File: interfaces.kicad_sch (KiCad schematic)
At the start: 120 parts, among them J6001 HDMI-A_WE_685119134923, J6002 USB-C_USB4105-GF-A, J6003 MicroSD_693071020811, Q6001 BSS138PW, Q6002 BSS138PW, Q6003 BSS138PW, Q6004 BSS138PW, Q6005 BSS138PW, Q6006 BSS138PW, Q6007 BSS138PW, Q6008 BSS138PW, SW6001 SW_KMR211NGLFS_SMD, U6001 FT4232H_VQFN, Y6001 Oscillator_SMD_12MHz_KX-7

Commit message: Sync new components with PCB
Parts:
- removed C? (x2): C_100n_0402_EIA, K410T-devboard-footprints:C_0402_1005Metric_EIA, symbol K410T-devboard:C_100n_0402_EIA
- removed FB?: FB_120Z_2A_0603, K410T-devboard-footprints:FB_0603_1608Metric, symbol K410T-devboard:FB_120Z_2A_0603
- added C6020, C6021: C_100n_0402, antmicro-footprints:C_0402_1005Metric, symbol antmicroCapacitors0402:C_100n_0402
- added FB6003: FB_120Z_2A_Murata-BLM18PG_0603, antmicro-footprints:FB_0603_1608Metric, symbol antmicroFerriteBeadsandChips:FB_120Z_2A_Murata-BLM18PG_0603
- gave numbers to parts that had none: 27
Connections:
- net +5V: now also FB6003.1
- net FTDI_3V3: now also C6021.2
- net GND: now also C6020.1, C6021.1
- net HDMI_5V: now also C6020.2, FB6003.2

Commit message: Continue optimizing placement and layout of misc. circuitry
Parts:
- added C6022, C6023, C6024, C6025: C_100n_0402, antmicro-footprints:C_0402_1005Metric, symbol antmicroCapacitors0402:C_100n_0402
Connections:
- net +3V3: now also C6024.2, C6025.2; no longer C6005.1, C6008.1, C6009.1, C6010.1
- net DBG_USB_N: now also U6004.4, U6004.7; no longer U6004.2, U6004.9
- net DBG_USB_P: now also U6004.2, U6004.9; no longer U6004.1, U6004.10
- net FTDI_3V3: now also C6005.1, C6008.1, C6009.1, C6010.1, C6022.2, C6023.2
- net FTDI_JTAG_TCK: now also U6003.3 (A2); no longer U6003.2 (A1)
- net FTDI_JTAG_TMS: now also U6003.2 (A1); no longer U6003.3 (A2)
- net GND: now also C6022.1, C6023.1, C6024.1, C6025.1
- net TCK_JTAG: now also R6011.2; no longer R6008.2
- net TMS_JTAG: now also R6008.2; no longer R6011.2
- new net: U6004.1, U6004.10

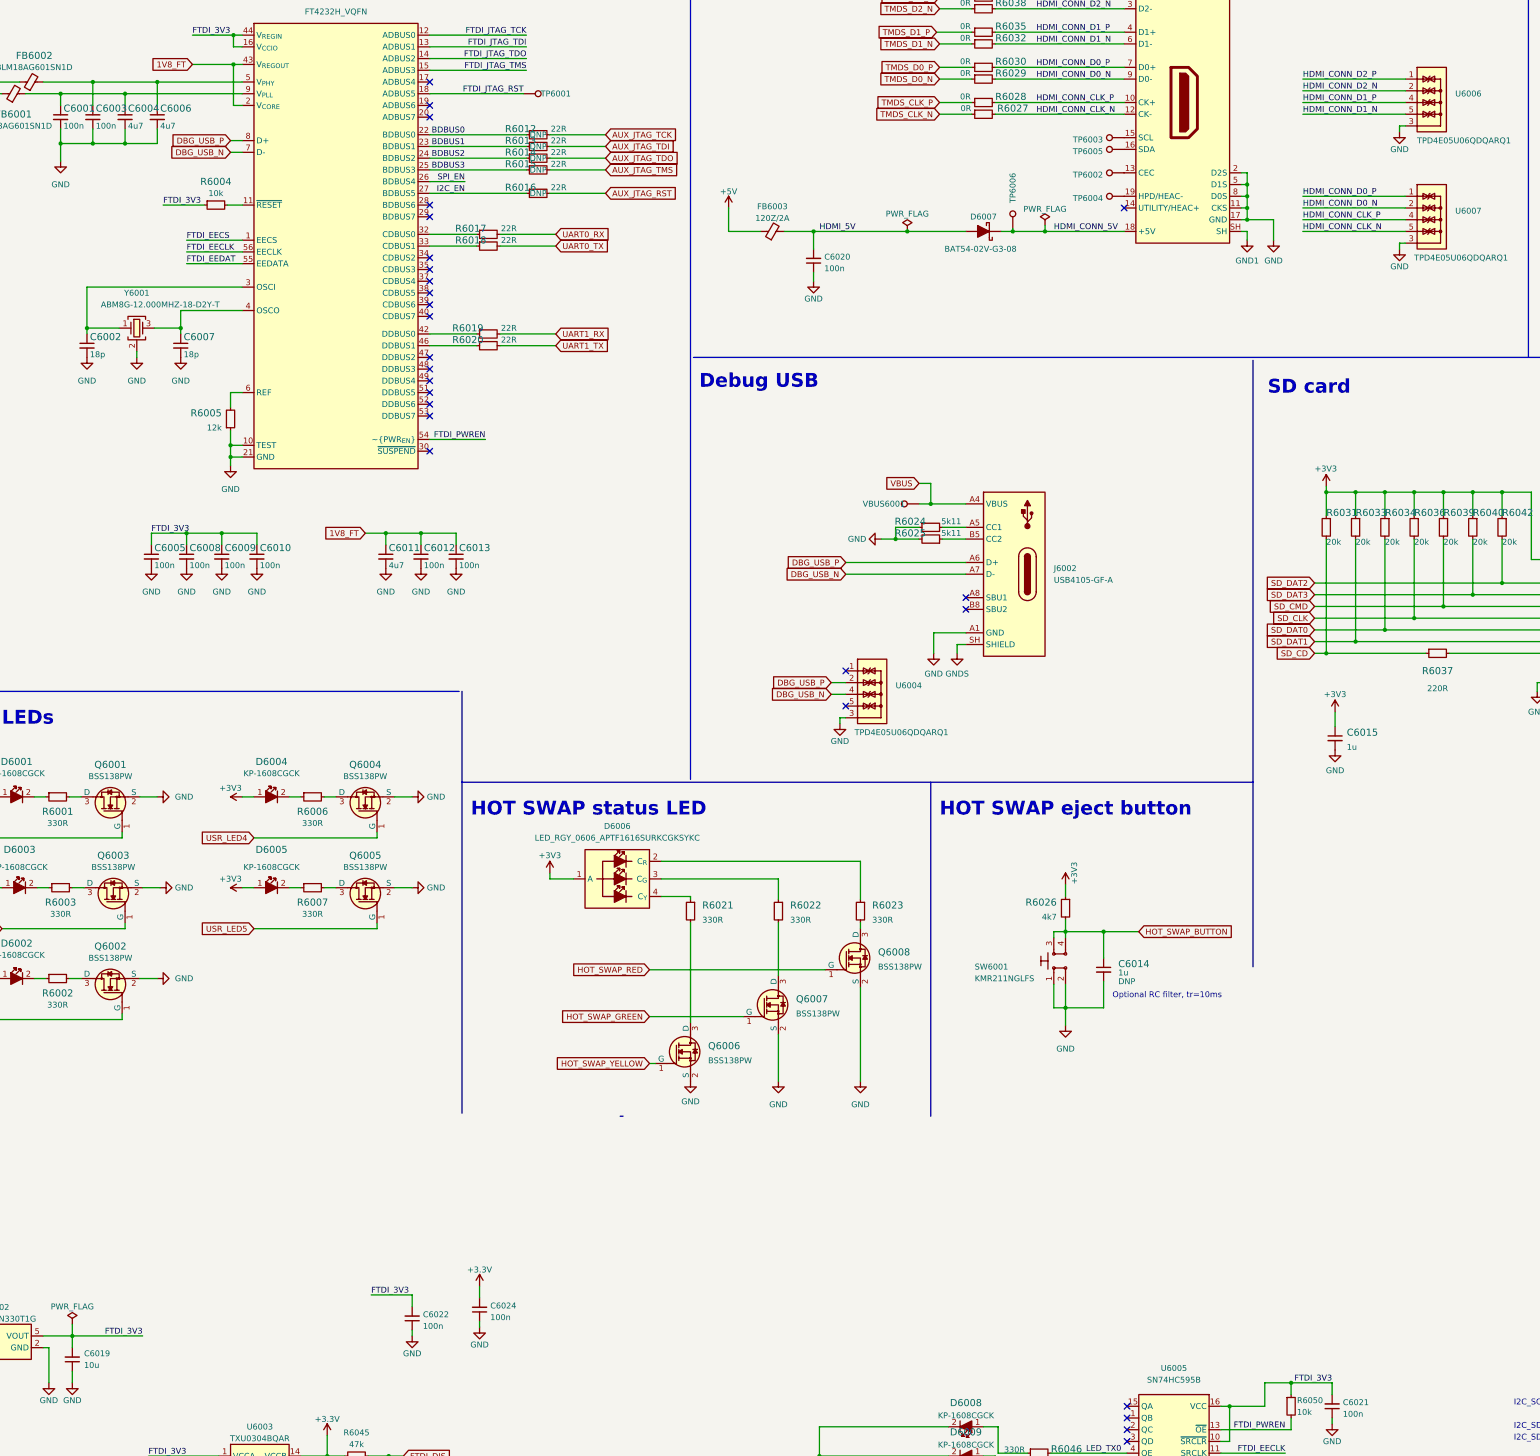
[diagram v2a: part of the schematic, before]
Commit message: Optimize BOM, replace obsolete parts, improve manufacturing attributes
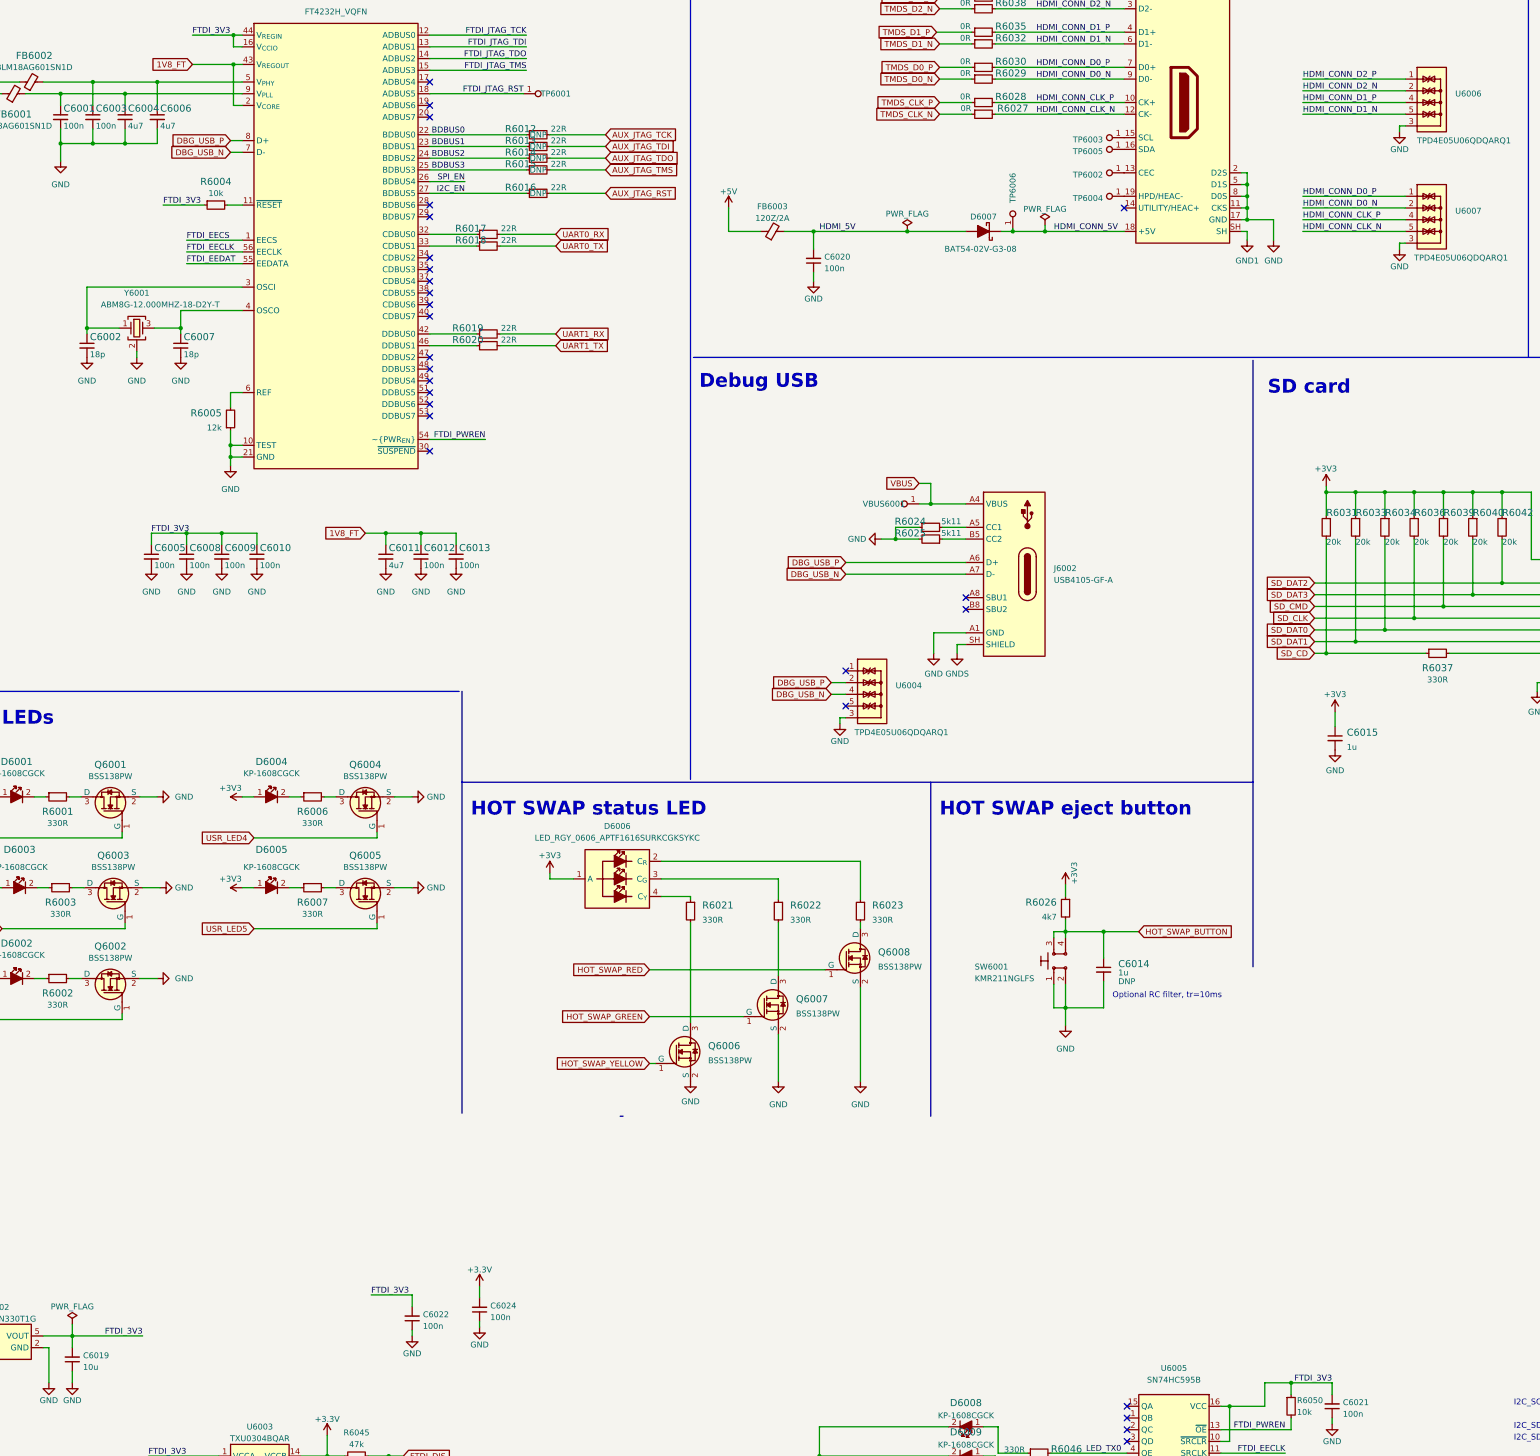
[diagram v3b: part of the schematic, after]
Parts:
- removed C6019: C_10u_0402, antmicro-footprints:C_0402_1005Metric, symbol antmicroCapacitors0402:C_10u_0402
- removed R6037: R_220R_0402, sodimm-ddr5-tester-footprints:R_0402_1005Metric, symbol sodimm-ddr5-tester:R_220R_0402
- added C6019: C_10u_6.3V_0402, antmicro-footprints:C_0402_1005Metric, symbol antmicroCapacitors0402:C_10u_6.3V_0402
- added R6037: R_330R_0402, sodimm-ddr5-tester-footprints:R_0402_1005Metric, symbol sodimm-ddr5-tester:R_330R_0402
- TP6001, TP6002, TP6003, TP6004, TP6005, TP6006, VBUS6001: footprint sodimm-ddr5-tester-footprints:Testpoint_smd_1mm -> antmicro-footprints:TP_SMD_1mm; symbol sodimm-ddr5-tester:TP_1mm_SMD -> antmicroTestPoints:TP_1mm_SMD
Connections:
- net FTDI_3V3: now also C6019.2
- net GND: now also C6019.1
- net SD_CD: now also R6037.1
- net at J6003.9 (CD_SW1): now also R6037.2

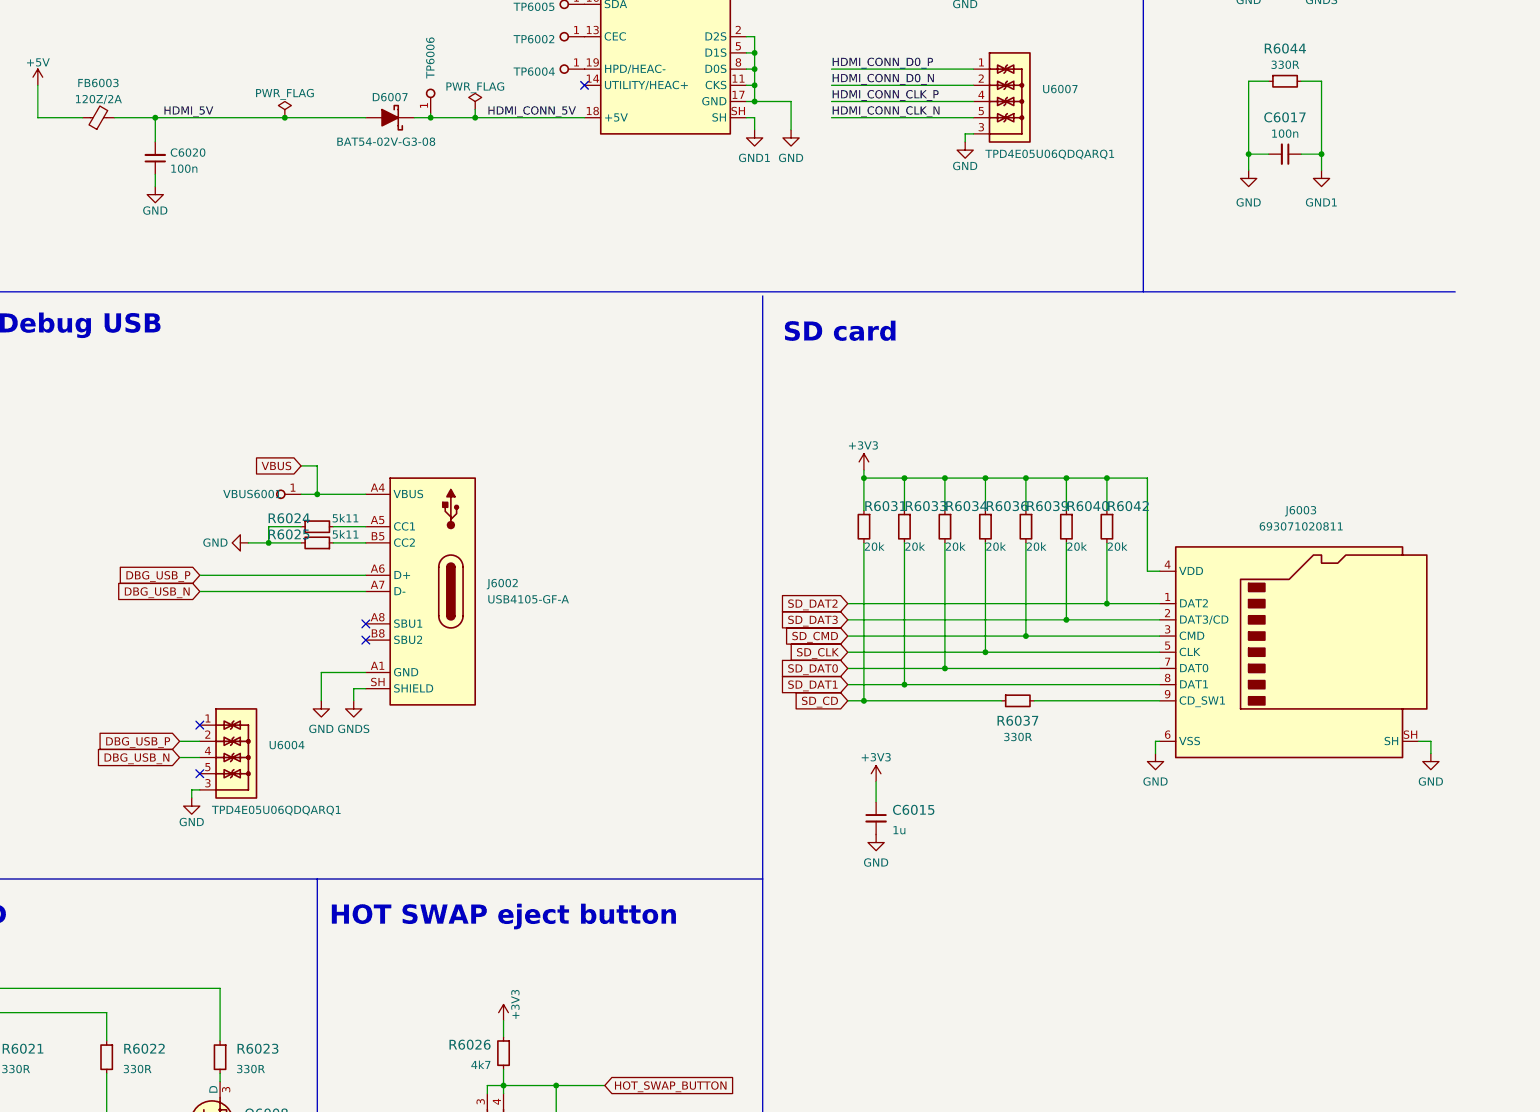
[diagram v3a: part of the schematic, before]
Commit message: Connect unused banks to 3V3 for better ESD protection, add ESD protection to SD card, add silkscreen markings
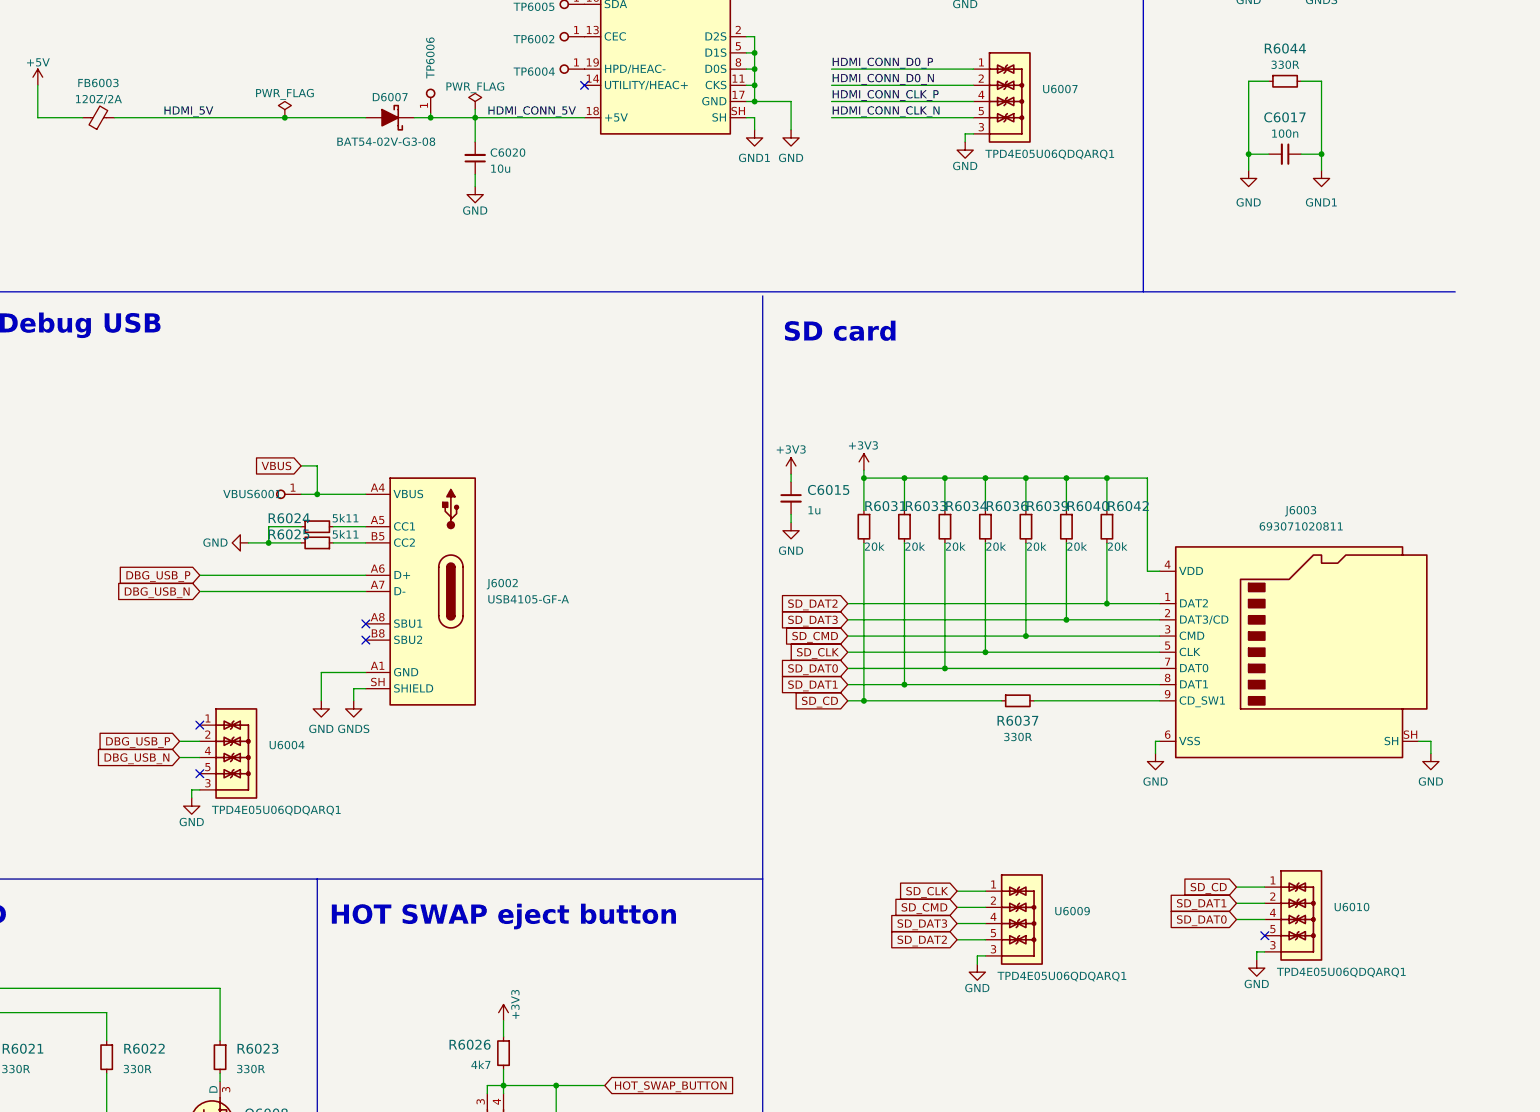
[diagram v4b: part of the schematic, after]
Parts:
- removed C6020: C_100n_0402, antmicro-footprints:C_0402_1005Metric, symbol antmicroCapacitors0402:C_100n_0402
- added C6020: C_10u_6.3V_0402, antmicro-footprints:C_0402_1005Metric, symbol antmicroCapacitors0402:C_10u_6.3V_0402
- added U6009, U6010: TPD4E05U06QDQARQ1, antmicro-footprints:USON-10_2.5x1mm_P0.5mm, symbol antmicroTVSDiodes:TPD4E05U06QDQARQ1
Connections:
- net GND: now also C6020.1, U6009.3, U6009.8, U6010.3, U6010.8
- net HDMI_CONN_5V: now also C6020.2
- net SD_CD: now also U6010.1, U6010.10
- net SD_CLK: now also U6009.1, U6009.10
- net SD_CMD: now also U6009.2, U6009.9
- net SD_DAT0: now also U6010.4, U6010.7
- net SD_DAT1: now also U6010.2, U6010.9
- net SD_DAT2: now also U6009.5, U6009.6
- net SD_DAT3: now also U6009.4, U6009.7
- new net: U6010.5, U6010.6
- no-connect marks 29 -> 30
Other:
- moved on the sheet: C6015
